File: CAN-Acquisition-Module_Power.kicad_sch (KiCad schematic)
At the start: 38 parts

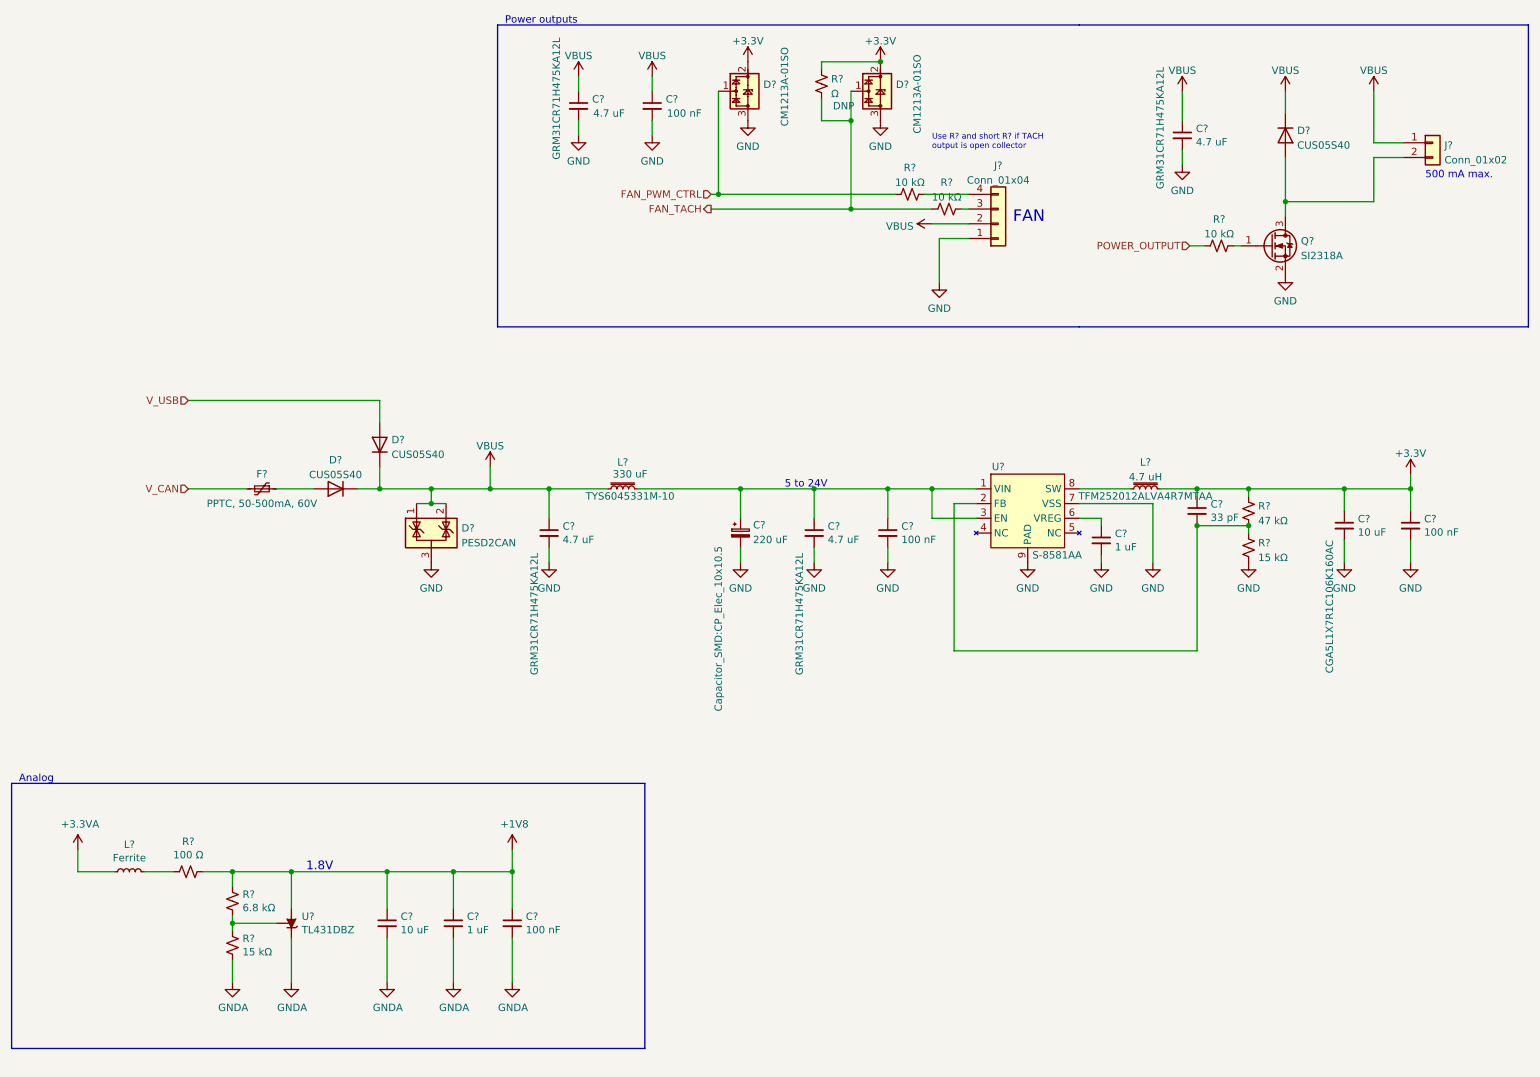
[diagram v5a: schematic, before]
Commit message: Added screen sections and annotations
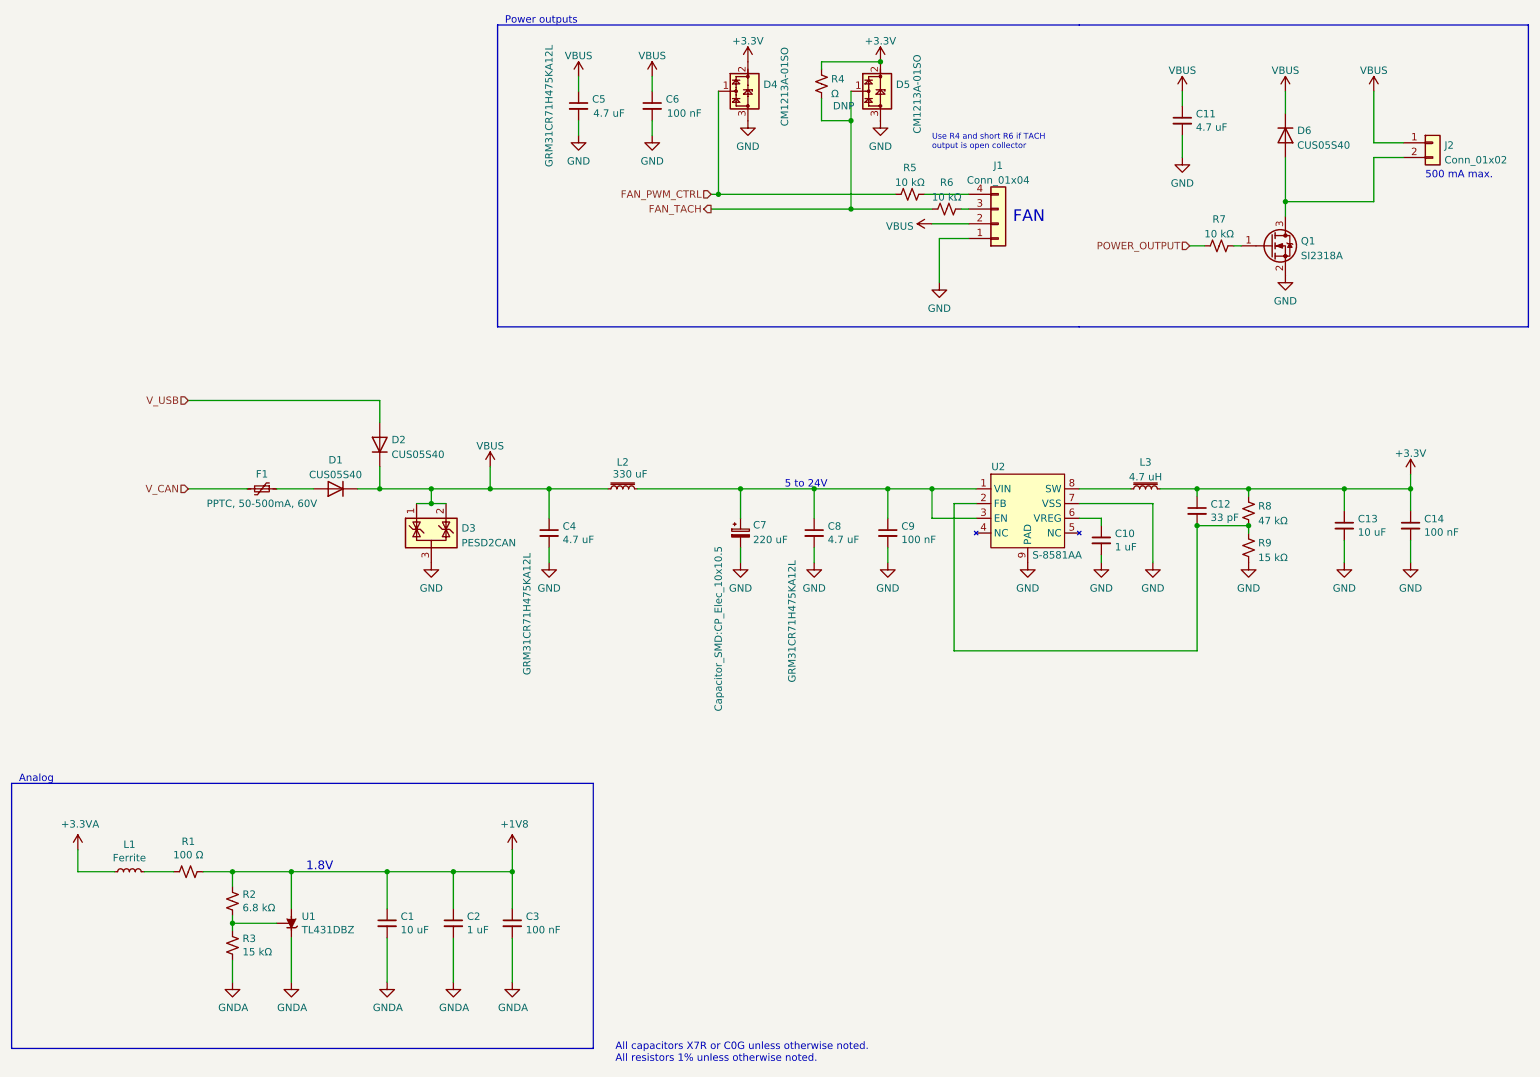
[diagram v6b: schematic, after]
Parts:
- C1: renamed from C?; footprint Capacitor_SMD:C_1206_3216Metric -> Capacitor_SMD:C_0805_2012Metric; Mfr. (none) -> TDK Corporation; P/N (none) -> C2012X7R0J106K125AB; Rated Voltage (none) -> 6.3V
- C10, C2: renamed from C?; Mfr. (none) -> Samsung Electro-Mechanics; P/N (none) -> CL10B105KA8NNNC; Rated Voltage (none) -> 25V
- C11, C4, C5, C8: renamed from C?; MPN GRM31CR71H475KA12L -> (none); Manufacturer Murata Electronics -> (none); Mfr. (none) -> Murata Electronics; P/N (none) -> GRM31CR71H475KA12L; Rated Voltage (none) -> 50V
- C13: renamed from C?; footprint Capacitor_SMD:C_1206_3216Metric -> Capacitor_SMD:C_0805_2012Metric; MPN CGA5L1X7R1C106K160AC -> (none); Manufacturer TDK Corporation -> (none); Mfr. (none) -> TDK Corporation; P/N (none) -> C2012X7R0J106K125AB; Rated Voltage (none) -> 6.3V
- C14, C3: renamed from C?; Mfr. (none) -> KYOCERA AVX; P/N (none) -> 0402YC104KAT2A; Rated Voltage (none) -> 16V
- C6, C9: renamed from C?; Mfr. (none) -> Samsung Electro-Mechanics; P/N (none) -> CL10B104KB8NNWC; Rated Voltage (none) -> 50V
- C7: renamed from C?; Mfr. (none) -> Kyocera; P/N (none) -> AEH1213221M050R; Rated Voltage (none) -> 50V
- L2: renamed from L?; MPN TYS6045331M-10 -> (none); P/N (none) -> TYS6045331M-10
- L3: renamed from L?; MPN TFM252012ALVA4R7MTAA -> (none); Mfr. (none) -> TDK Corporation; P/N (none) -> TFM252012ALVA4R7MTAA
- gave numbers to parts that had none: 23
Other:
- note added: "All capacitors X7R or C0G unless otherwise noted. All resistors 1% unless otherwise noted."
- note added: "Use R4 and short R6 if TACH output is open collector"
- note removed: "Use R? and short R? if TACH output is open collector"
- moved on the sheet: C11

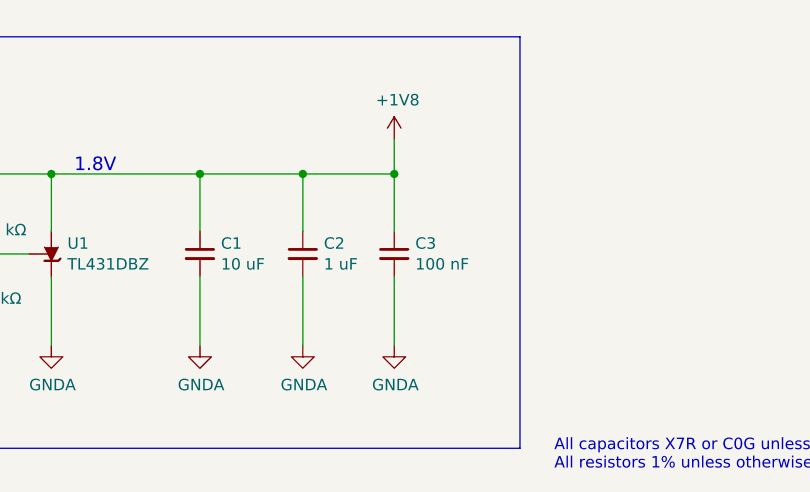
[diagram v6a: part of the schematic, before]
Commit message: Layout of analog section started
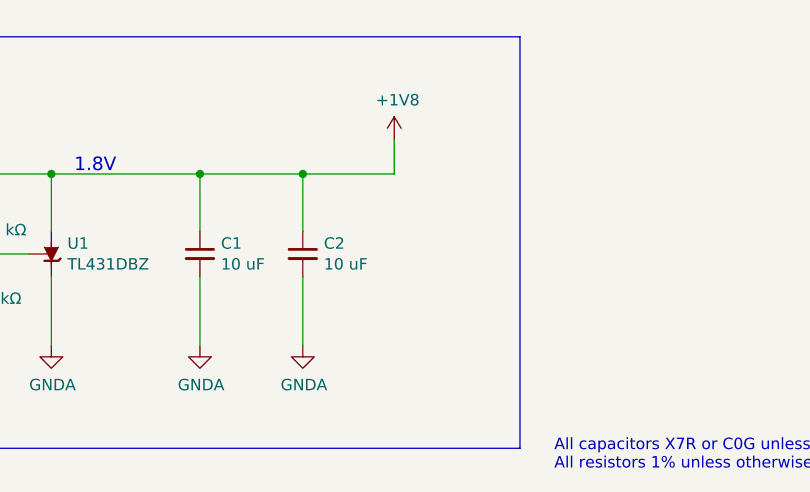
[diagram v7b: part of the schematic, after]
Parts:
- removed C3: 100 nF, Capacitor_SMD:C_0402_1005Metric, symbol Device:C_Small
- C2: value 1 uF -> 10 uF; footprint Capacitor_SMD:C_0603_1608Metric -> Capacitor_SMD:C_0805_2012Metric; Mfr. Samsung Electro-Mechanics -> TDK Corporation; P/N CL10B105KA8NNNC -> C2012X7R0J106K125AB; Rated Voltage 25V -> 6.3V
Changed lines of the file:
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@@
   (junction (at 163.83 31.75) (diameter 0) (color 0 0 0 0)
   )
-  (junction (at 105.41 161.29) (diameter 0) (color 0 0 0 0)
-  )
   (junction (at 111.76 95.25) (diameter 0) (color 0 0 0 0)
   )
@@
     (stroke (width 0) (type default) (color 0 0 0 0))
   )
-  (wire (pts (xy 105.41 167.64) (xy 105.41 161.29))
-    (stroke (width 0) (type default) (color 0 0 0 0))
-  )
   (wire (pts (xy 105.41 161.29) (xy 95.25 161.29))
     (stroke (width 0) (type default) (color 0 0 0 0))
@@
     (stroke (width 0) (type default) (color 0 0 0 0))
   )
+  (wire (pts (xy 95.25 172.72) (xy 95.25 180.34))
+    (stroke (width 0) (type default) (color 0 0 0 0))
+  )
   (wire (pts (xy 157.48 95.25) (xy 157.48 100.33))
     (stroke (width 0) (type default) (color 0 0 0 0))
@@
     (stroke (width 0) (type default) (color 0 0 0 0))
   )
-  (wire (pts (xy 95.25 172.72) (xy 95.25 180.34))
-    (stroke (width 0) (type default) (color 0 0 0 0))
-  )
   (polyline (pts (xy 102.87 15.24) (xy 102.87 17.78))
     (stroke (width 0) (type default) (color 0 0 0 0))
@@
   )
   (wire (pts (xy 179.07 52.07) (xy 184.15 52.07))
-    (stroke (width 0) (type default) (color 0 0 0 0))
-  )
-  (wire (pts (xy 105.41 172.72) (xy 105.41 180.34))
     (stroke (width 0) (type default) (color 0 0 0 0))
   )
@@
     )
     (property "Datasheet" "" (id 3) (at 83.82 180.34 0)
-      (effects (font (size 1.27 1.27)) hide)
-    )
-    (pin "1")
-  )
-  (symbol (lib_id "Device:C_Small") (at 95.25 170.18 0) (unit 1)
-    (in_bom yes) (on_board yes)
-    (property "Reference" "C2" (id 0) (at 97.5868 169.0116 0)
-      (effects (font (size 1.27 1.27)) (justify left))
-    )
-    (property "Value" "1 uF" (id 1) (at 97.5868 171.323 0)
-      (effects (font (size 1.27 1.27)) (justify left))
-    )
-    (property "Footprint" "Capacitor_SMD:C_0603_1608Metric" (id 2) (at 95.25 170.18 0)
-      (effects (font (size 1.27 1.27)) hide)
-    )
-    (property "Datasheet" "~" (id 3) (at 95.25 170.18 0)
-      (effects (font (size 1.27 1.27)) hide)
-    )
-    (property "Mfr." "Samsung Electro-Mechanics " (id 4) (at 95.25 170.18 0)
-      (effects (font (size 1.27 1.27)) hide)
-    )
-    (property "P/N" "CL10B105KA8NNNC" (id 5) (at 95.25 170.18 0)
-      (effects (font (size 1.27 1.27)) hide)
-    )
-    (property "Rated Voltage" "25V" (id 6) (at 95.25 170.18 0)
-      (effects (font (size 1.27 1.27)) hide)
-    )
-    (pin "1")
-    (pin "2")
-  )
-  (symbol (lib_id "Device:C_Small") (at 105.41 170.18 0) (unit 1)
-    (in_bom yes) (on_board yes)
-    (property "Reference" "C3" (id 0) (at 107.7468 169.0116 0)
-      (effects (font (size 1.27 1.27)) (justify left))
-    )
-    (property "Value" "100 nF" (id 1) (at 107.7468 171.323 0)
-      (effects (font (size 1.27 1.27)) (justify left))
-    )
-    (property "Footprint" "Capacitor_SMD:C_0402_1005Metric" (id 2) (at 105.41 170.18 0)
-      (effects (font (size 1.27 1.27)) hide)
-    )
-    (property "Datasheet" "~" (id 3) (at 105.41 170.18 0)
-      (effects (font (size 1.27 1.27)) hide)
-    )
-    (property "Mfr." "KYOCERA AVX " (id 4) (at 105.41 170.18 0)
-      (effects (font (size 1.27 1.27)) hide)
-    )
-    (property "P/N" "0402YC104KAT2A" (id 5) (at 105.41 170.18 0)
-      (effects (font (size 1.27 1.27)) hide)
-    )
-    (property "Rated Voltage" "16V" (id 6) (at 105.41 170.18 0)
-      (effects (font (size 1.27 1.27)) hide)
-    )
-    (pin "1")
-    (pin "2")
-  )
-  (symbol (lib_id "power:GNDA") (at 95.25 180.34 0) (unit 1)
-    (in_bom yes) (on_board yes)
-    (property "Reference" "#PWR06" (id 0) (at 95.25 186.69 0)
-      (effects (font (size 1.27 1.27)) hide)
-    )
-    (property "Value" "GNDA" (id 1) (at 95.377 184.7342 0))
-    (property "Footprint" "" (id 2) (at 95.25 180.34 0)
-      (effects (font (size 1.27 1.27)) hide)
-    )
-    (property "Datasheet" "" (id 3) (at 95.25 180.34 0)
-      (effects (font (size 1.27 1.27)) hide)
-    )
-    (pin "1")
-  )
-  (symbol (lib_id "power:GNDA") (at 105.41 180.34 0) (unit 1)
-    (in_bom yes) (on_board yes)
-    (property "Reference" "#PWR09" (id 0) (at 105.41 186.69 0)
-      (effects (font (size 1.27 1.27)) hide)
-    )
-    (property "Value" "GNDA" (id 1) (at 105.537 184.7342 0))
-    (property "Footprint" "" (id 2) (at 105.41 180.34 0)
-      (effects (font (size 1.27 1.27)) hide)
-    )
-    (property "Datasheet" "" (id 3) (at 105.41 180.34 0)
       (effects (font (size 1.27 1.27)) hide)
     )
@@
     (pin "3")
   )
+  (symbol (lib_id "Device:C_Small") (at 95.25 170.18 0) (unit 1)
+    (in_bom yes) (on_board yes)
+    (property "Reference" "C2" (id 0) (at 97.5868 169.0116 0)
+      (effects (font (size 1.27 1.27)) (justify left))
+    )
+    (property "Value" "10 uF" (id 1) (at 97.5868 171.323 0)
+      (effects (font (size 1.27 1.27)) (justify left))
+    )
+    (property "Footprint" "Capacitor_SMD:C_0805_2012Metric" (id 2) (at 95.25 170.18 0)
+      (effects (font (size 1.27 1.27)) hide)
+    )
+    (property "Datasheet" "~" (id 3) (at 95.25 170.18 0)
+      (effects (font (size 1.27 1.27)) hide)
+    )
+    (property "Mfr." "TDK Corporation " (id 4) (at 95.25 170.18 0)
+      (effects (font (size 1.27 1.27)) hide)
+    )
+    (property "P/N" "C2012X7R0J106K125AB" (id 5) (at 95.25 170.18 0)
+      (effects (font (size 1.27 1.27)) hide)
+    )
+    (property "Rated Voltage" "6.3V" (id 6) (at 95.25 170.18 0)
+      (effects (font (size 1.27 1.27)) hide)
+    )
+    (pin "1")
+    (pin "2")
+  )
   (symbol (lib_id "power:GND") (at 116.84 34.29 0) (unit 1)
     (in_bom yes) (on_board yes) (fields_autoplaced)
@@
     (pin "2")
   )
+  (symbol (lib_id "power:GNDA") (at 95.25 180.34 0) (unit 1)
+    (in_bom yes) (on_board yes)
+    (property "Reference" "#PWR?" (id 0) (at 95.25 186.69 0)
+      (effects (font (size 1.27 1.27)) hide)
+    )
+    (property "Value" "GNDA" (id 1) (at 95.377 184.7342 0))
+    (property "Footprint" "" (id 2) (at 95.25 180.34 0)
+      (effects (font (size 1.27 1.27)) hide)
+    )
+    (property "Datasheet" "" (id 3) (at 95.25 180.34 0)
+      (effects (font (size 1.27 1.27)) hide)
+    )
+    (pin "1")
+  )
   (symbol (lib_id "Device:R_Small_US") (at 232.41 105.41 0) (unit 1)

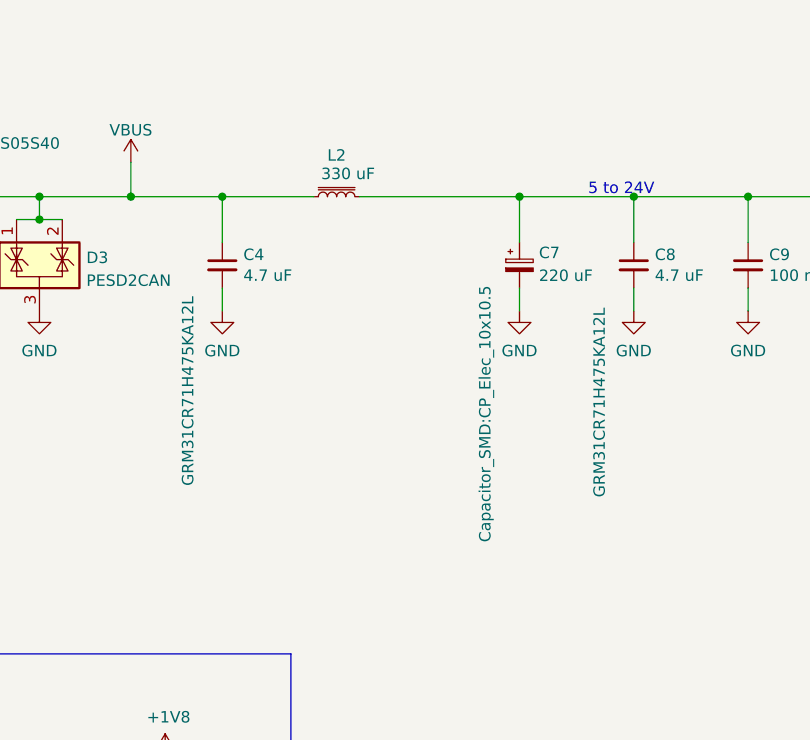
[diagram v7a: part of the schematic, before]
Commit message: Analog section, screen and USB finished
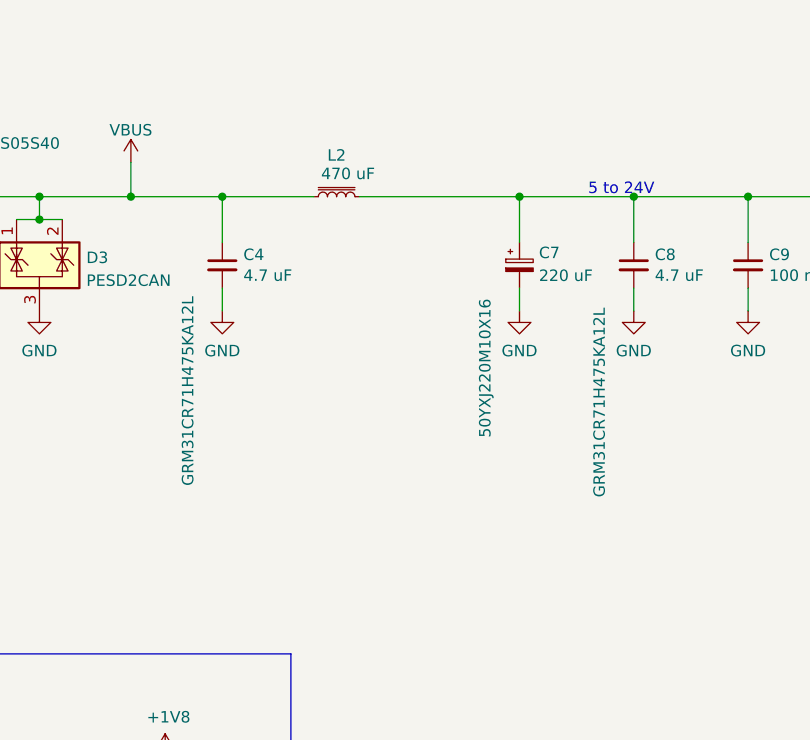
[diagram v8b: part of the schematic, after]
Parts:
- C7: footprint Capacitor_SMD:CP_Elec_10x10.5 -> Capacitor_THT:CP_Radial_D10.0mm_P5.00mm; Mfr. Kyocera -> Rubycon; P/N AEH1213221M050R -> 50YXJ220M10X16
- L2: value 330 uF -> 470 uF; footprint Inductor_SMD:L_Bourns_SRN6045TA -> CAN-Acquisition-Module:Murata_LQH43_1812(4532_Metric); P/N TYS6045331M-10 -> LQH43CN471K03L
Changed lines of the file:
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@@
     (in_bom yes) (on_board yes)
     (property "Reference" "L2" (id 0) (at 124.46 90.6612 90))
-    (property "Value" "330 uF" (id 1) (at 125.73 92.71 90))
-    (property "Footprint" "Inductor_SMD:L_Bourns_SRN6045TA" (id 2) (at 124.46 95.25 0)
-      (effects (font (size 1.27 1.27)) hide)
-    )
-    (property "Datasheet" "https://www.laird.com/sites/default/files/tys6045-series-datasheet.pdf" (id 3) (at 124.46 95.25 0)
-      (effects (font (size 1.27 1.27)) hide)
-    )
-    (property "P/N" "TYS6045331M-10" (id 4) (at 124.46 95.25 0)
+    (property "Value" "470 uF" (id 1) (at 125.73 92.71 90))
+    (property "Footprint" "CAN-Acquisition-Module:Murata_LQH43_1812(4532_Metric)" (id 2) (at 124.46 95.25 0)
+      (effects (font (size 1.27 1.27)) hide)
+    )
+    (property "Datasheet" "https://search.murata.co.jp/Ceramy/image/img/P02/JELF243A-0042.pdf" (id 3) (at 124.46 95.25 0)
+      (effects (font (size 1.27 1.27)) hide)
+    )
+    (property "P/N" "LQH43CN471K03L" (id 4) (at 124.46 95.25 0)
       (effects (font (size 1.27 1.27)) hide)
     )
@@
   (symbol (lib_id "power:GNDA") (at 95.25 180.34 0) (unit 1)
     (in_bom yes) (on_board yes)
-    (property "Reference" "#PWR?" (id 0) (at 95.25 186.69 0)
+    (property "Reference" "#PWR0193" (id 0) (at 95.25 186.69 0)
       (effects (font (size 1.27 1.27)) hide)
     )
@@
       (effects (font (size 1.27 1.27)) (justify left))
     )
-    (property "Footprint" "Capacitor_SMD:CP_Elec_10x10.5" (id 2) (at 140.97 119.38 90))
-    (property "Datasheet" "~" (id 3) (at 144.78 102.87 0)
-      (effects (font (size 1.27 1.27)) hide)
-    )
-    (property "Mfr." "Kyocera" (id 4) (at 144.78 102.87 0)
-      (effects (font (size 1.27 1.27)) hide)
-    )
-    (property "P/N" "AEH1213221M050R" (id 5) (at 144.78 102.87 0)
-      (effects (font (size 1.27 1.27)) hide)
-    )
+    (property "Footprint" "Capacitor_THT:CP_Radial_D10.0mm_P5.00mm" (id 2) (at 140.97 119.38 90)
+      (effects (font (size 1.27 1.27)) hide)
+    )
+    (property "Datasheet" "https://www.rubycon.co.jp/wp-content/uploads/catalog-aluminum/YXJ.pdf" (id 3) (at 144.78 102.87 0)
+      (effects (font (size 1.27 1.27)) hide)
+    )
+    (property "Mfr." "Rubycon" (id 4) (at 144.78 102.87 0)
+      (effects (font (size 1.27 1.27)) hide)
+    )
+    (property "P/N" "50YXJ220M10X16" (id 5) (at 140.97 114.3 90))
     (property "Rated Voltage" "50V" (id 6) (at 144.78 102.87 0)
       (effects (font (size 1.27 1.27)) hide)
